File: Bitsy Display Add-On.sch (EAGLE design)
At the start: 13 parts, among them IC1 APX803, SW1 KMR2

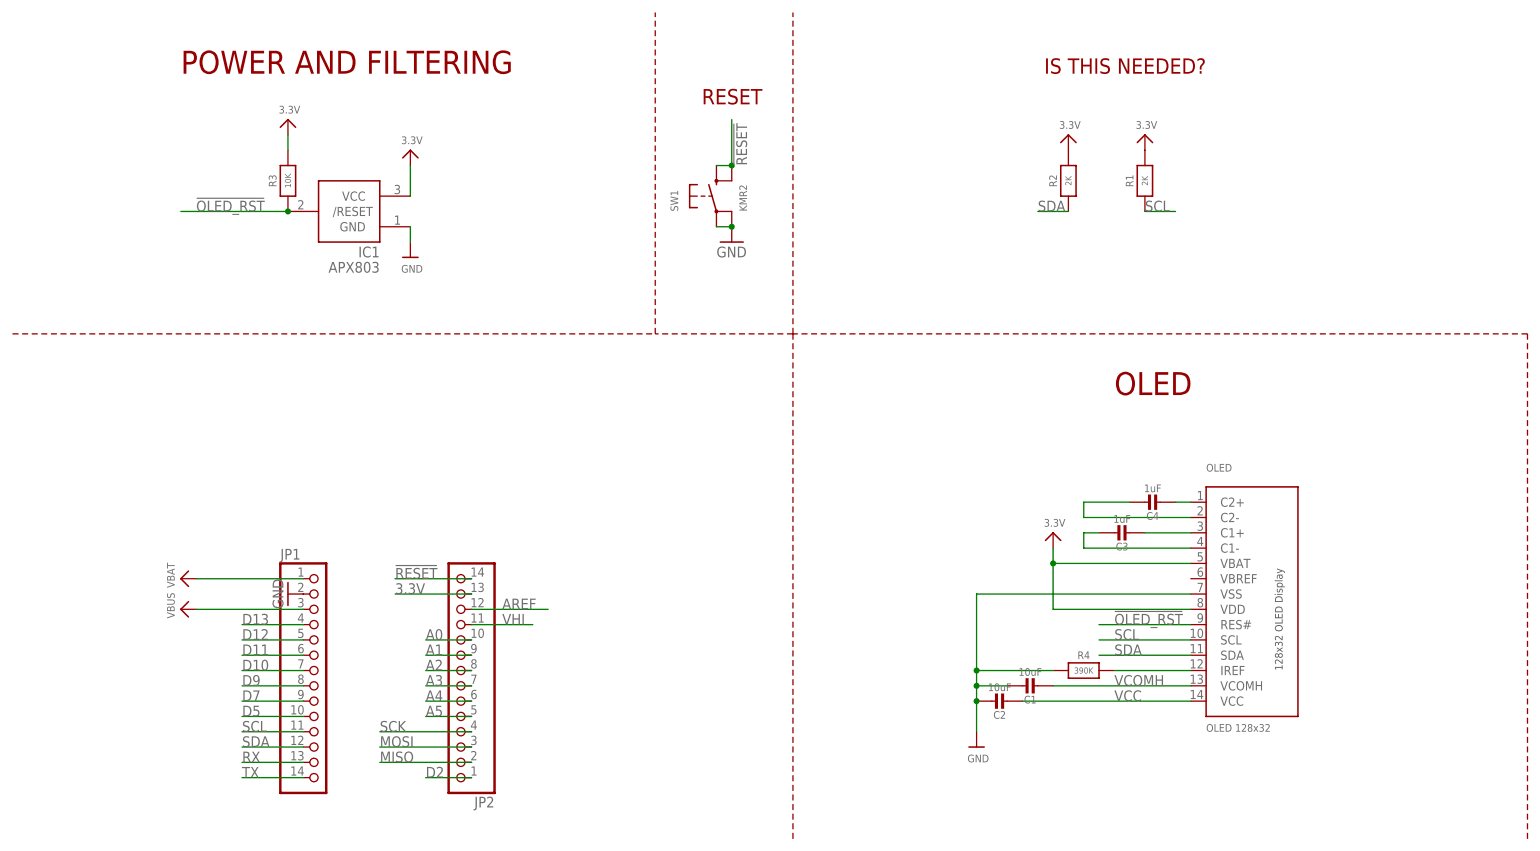
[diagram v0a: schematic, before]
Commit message: PCB Redisgned
Resistors and Capacitors on bottom of board
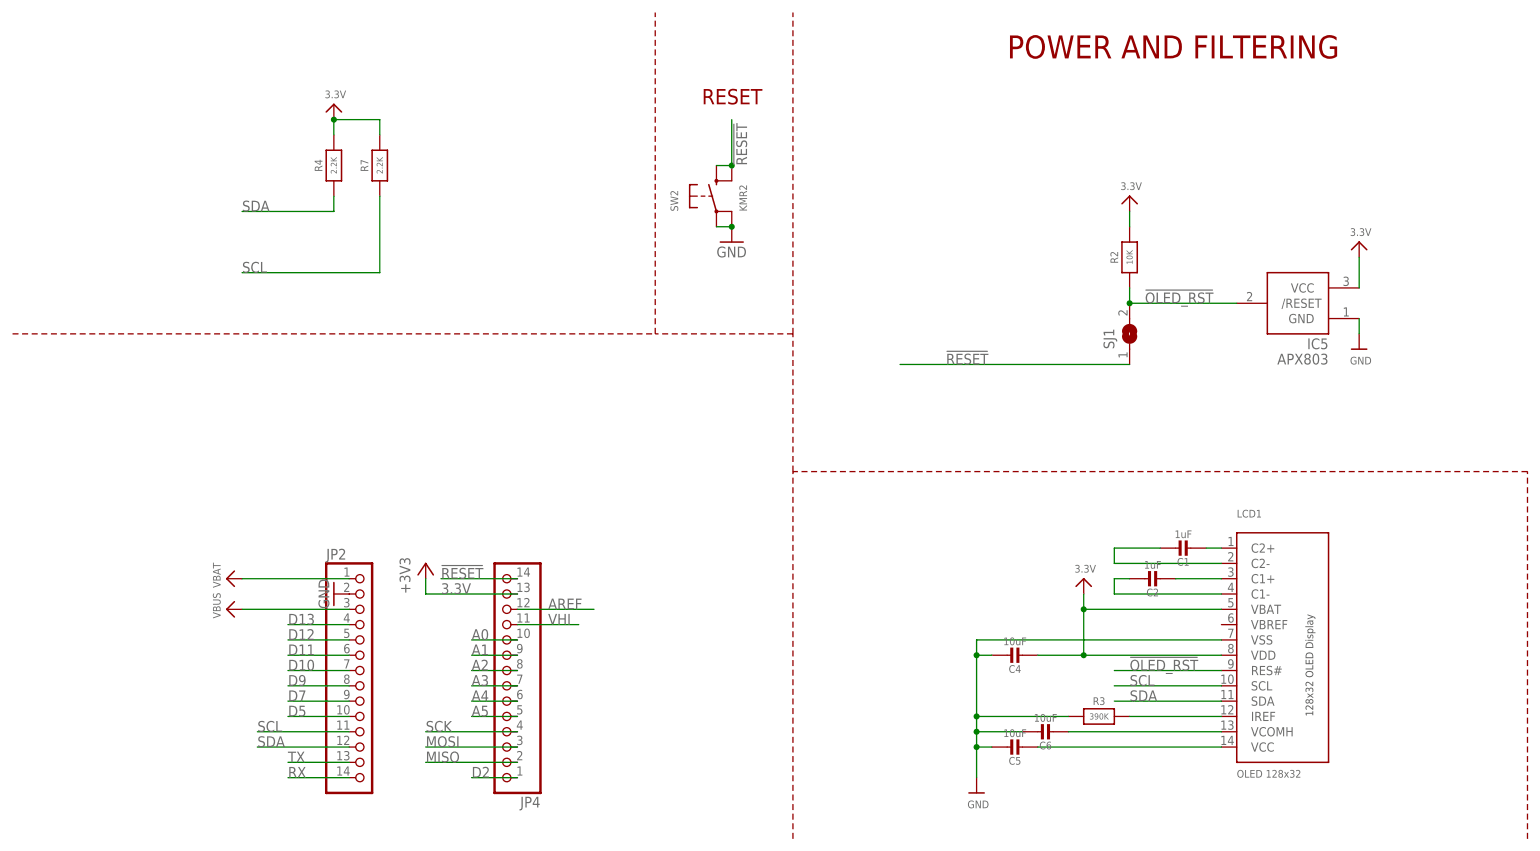
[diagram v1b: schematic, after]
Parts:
- removed C3: 1uF, microbuilder:CAP_CERAMIC0603_NO
- removed IC1: APX803, adafruit:AXP083-SAG
- removed JP1: (no value), microbuilder:HEADER-1X14
- removed OLED: OLED 128x32, microbuilder:DISP_OLED_UG-2832HSWEG02
- removed R1: 2K, microbuilder:RESISTOR_0402
- added C5, C6: 10uF, microbuilder:CAP_CERAMIC0805-NOOUTLINE
- added IC5: APX803, adafruit:AXP083-SAG
- added JP4: (no value), microbuilder:HEADER-1X14
- added LCD1: OLED 128x32, microbuilder:DISP_OLED_UG-2832HSWEG02
- added R7: 2.2K, microbuilder:RESISTOR0805_NOOUTLINE
- added SJ1: (no value), microbuilder:SOLDERJUMPER
- C1, C2: value 10uF -> 1uF
- C4: value 1uF -> 10uF; device microbuilder:CAP_CERAMIC0603_NO -> microbuilder:CAP_CERAMIC0805-NOOUTLINE
- R2: value 2K -> 10K; device microbuilder:RESISTOR_0402 -> microbuilder:RESISTOR_0805MP
- R3: value 10K -> 390K; device microbuilder:RESISTOR_0402 -> microbuilder:RESISTOR0805_NOOUTLINE
- R4: value 390K -> 2.2K; device microbuilder:RESISTOR_0603_NOOUT -> microbuilder:RESISTOR0805_NOOUTLINE
- renumbered SW1 to SW2
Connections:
- removed net VCC: C2.2, OLED.VCC
- removed net VCOMH: C1.2, OLED.VCOMH
- new net N$5: C6.2, LCD1.VCOMH
- new net N$6: C5.2, LCD1.VCC
- net !OLED_RST: now also IC5./RESET, LCD1.RES#, R2.1, SJ1.2; no longer IC1./RESET, OLED.RES#, R3.1
- net !RESET: now also JP4.14, SJ1.1; no longer JP2.14
- net 3.3V: now also C4.2, IC5.VCC, JP4.13, LCD1.VBAT, LCD1.VDD, R4.2, R7.2; no longer IC1.VCC, JP2.13, OLED.VBAT, OLED.VDD, R1.2, R3.2
- net A0: now also JP4.10; no longer JP2.10
- net A1: now also JP4.9; no longer JP2.9
- net A2: now also JP4.8; no longer JP2.8
- net A3: now also JP4.7; no longer JP2.7
- net A4: now also JP4.6; no longer JP2.6
- net A5: now also JP4.5; no longer JP2.5
- net AREF: now also JP4.12; no longer JP2.12
- net D10: now also JP2.7; no longer JP1.7
- net D11: now also JP2.6; no longer JP1.6
- net D12: now also JP2.5; no longer JP1.5
- net D13: now also JP2.4; no longer JP1.4
- net D2: now also JP4.1; no longer JP2.1
- net D5: now also JP2.10; no longer JP1.10
- net D7: now also JP2.9; no longer JP1.9
- net D9: now also JP2.8; no longer JP1.8
- net GND: now also C4.1, C5.1, C6.1, IC5.GND, JP2.2, LCD1.VSS, R3.1; no longer C1.1, C2.1, IC1.GND, JP1.2, OLED.VSS, R4.1
- net MISO: now also JP4.2; no longer JP2.2
- net MOSI: now also JP4.3; no longer JP2.3
- net N$1: now also C1.2, LCD1.C2+; no longer C4.2, OLED.C2+
- net N$2: now also C1.1, LCD1.C2-; no longer C4.1, OLED.C2-
- net N$3: now also C2.2, LCD1.C1+; no longer C3.2, OLED.C1+
- net N$4: now also C2.1, LCD1.C1-; no longer C3.1, OLED.C1-
- net N$7: now also LCD1.IREF, R3.2; no longer OLED.IREF, R4.2
- net RX: now also JP2.14; no longer JP1.13
- net SCK: now also JP4.4; no longer JP2.4
- net SCL: now also JP2.11, LCD1.SCL, R7.1; no longer JP1.11, OLED.SCL, R1.1
- net SDA: now also JP2.12, LCD1.SDA, R4.1; no longer JP1.12, OLED.SDA, R2.1
- net TX: now also JP2.13; no longer JP1.14
- net VBAT: now also JP2.1; no longer JP1.1
- net VBUS: now also JP2.3; no longer JP1.3
- net VHI: now also JP4.11; no longer JP2.11
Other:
- note removed: "IS THIS NEEDED?"
- note removed: "OLED"
- moved on the sheet: C1, C2, C4, JP2, R2, R3, R4
